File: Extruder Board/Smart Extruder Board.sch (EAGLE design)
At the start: 15 parts

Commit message: BCN3D Electronics REV.E tested and manufactured
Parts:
- removed FFC1: FFC_20V_90G_1MM", MarcEagleParts:FFC_20V_90G_1MM"
- removed HALL: (no value), adafruit:JST_3PIN
- removed HOTEND: (no value), MarcEagleParts:JST_4PIN
- removed TP1, TP2, TP3, TP4, TP7: TPB1,27, testpad:TPB1,27
- added CN1: (no value), MarcEagleParts:JST_4PINPA
- added ENDSTOP: (no value), SparkFun-Connectors:JST_2MM_MALE
- added VERT_FFC1: FFC_20V_90G_1MM3, MarcEagleParts:FFC_20V_90G_1MM3
- CFAN, LFAN: MF (none) -> JST (JAPAN SOLDERLESS TERMINALS); MPN (none) -> S2B-PH-SM4-TB(LF)(SN); OC_FARNELL (none) -> 9492615
- TP5, TP6, U$1, U$2, U$3: OC_FARNELL (none) -> unknown
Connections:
- removed net ATLVL: FFC1.20, HALL.2, TP4.TP
- new net GNDTHERM: CN1.4, VERT_FFC1.2
- new net Z-ENDSTOP: ENDSTOP.+, VERT_FFC1.20
- net +24V: now also CN1.1, VERT_FFC1.10, VERT_FFC1.12, VERT_FFC1.18, VERT_FFC1.19, VERT_FFC1.8; no longer FFC1.10, FFC1.12, FFC1.18, FFC1.19, FFC1.8, HOTEND.1
- net +5V: now also VERT_FFC1.1; no longer FFC1.1, HALL.3
- net GND: now also ENDSTOP.-, VERT_FFC1.11, VERT_FFC1.17, VERT_FFC1.4, VERT_FFC1.7, VERT_FFC1.9, VERT_FFC1.GND@1, VERT_FFC1.GND@2; no longer FFC1.11, FFC1.17, FFC1.2, FFC1.4, FFC1.7, FFC1.9, FFC1.GND@2, FFC1.GND|1, HALL.1, HOTEND.4, TP7.TP
- net HOTEND: now also CN1.2, VERT_FFC1.13, VERT_FFC1.14, VERT_FFC1.15, VERT_FFC1.16; no longer FFC1.13, FFC1.14, FFC1.15, FFC1.16, HOTEND.2, TP3.TP
- net HOTEND_THERM: now also CN1.3, VERT_FFC1.3; no longer FFC1.3, HOTEND.3, TP1.TP
- net LFAN: now also VERT_FFC1.5, VERT_FFC1.6; no longer FFC1.5, FFC1.6, TP2.TP
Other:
- note added: "D"
- note removed: "B"

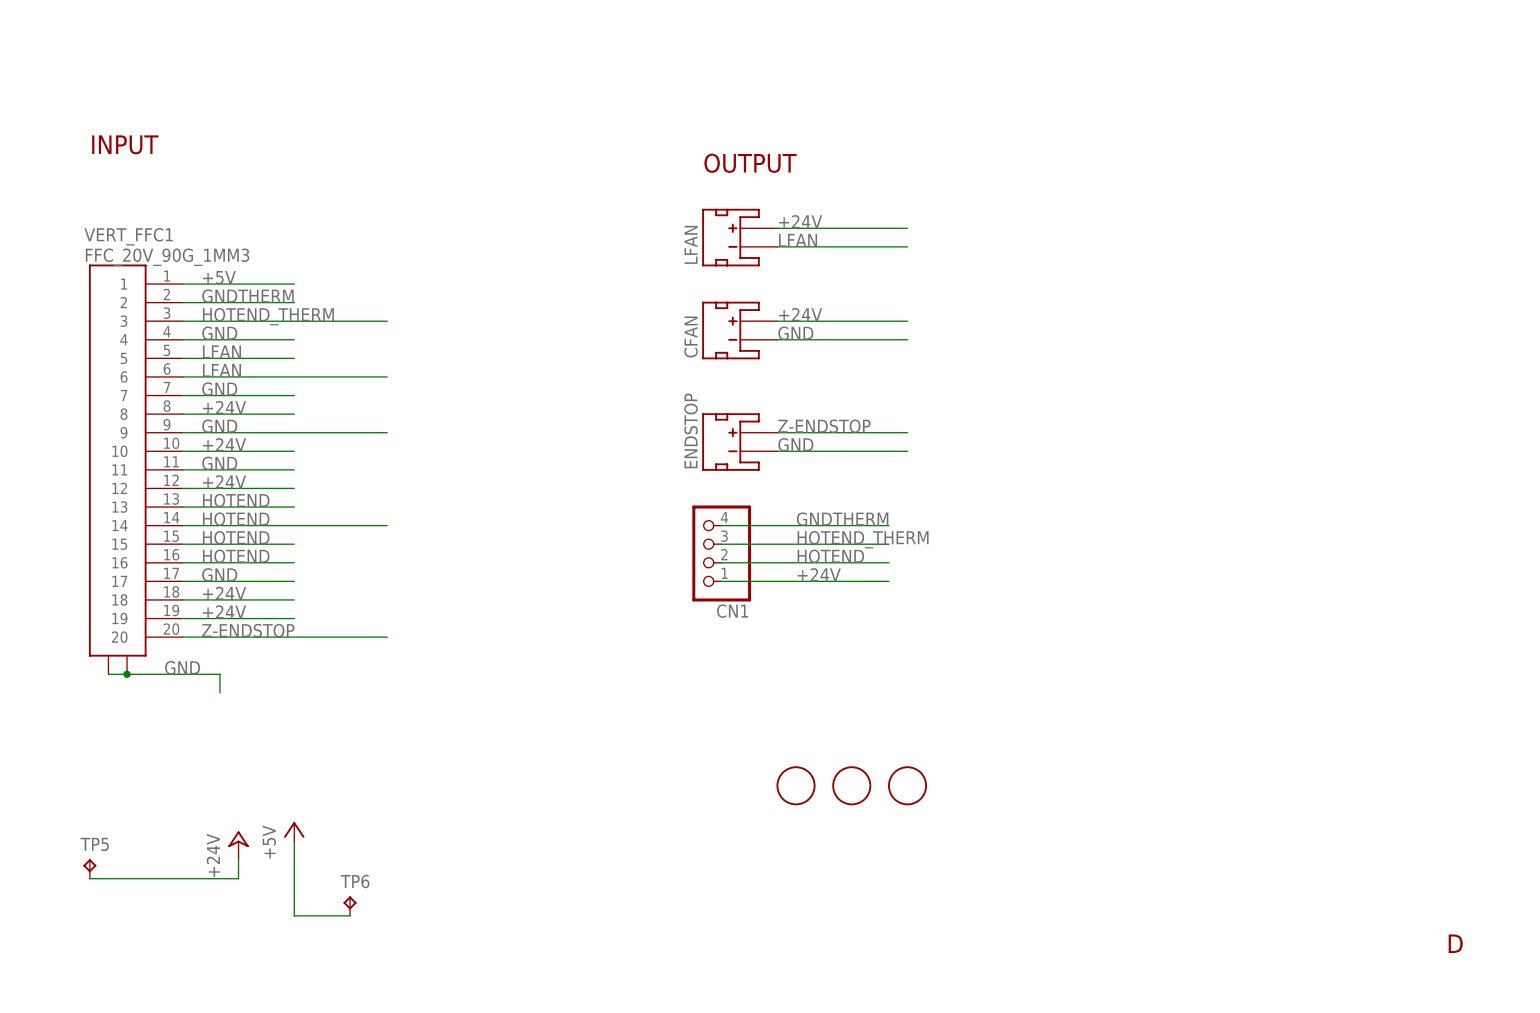
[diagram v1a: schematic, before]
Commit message: File for the REV.H
Files from the REV.H Released with new and more documentation.
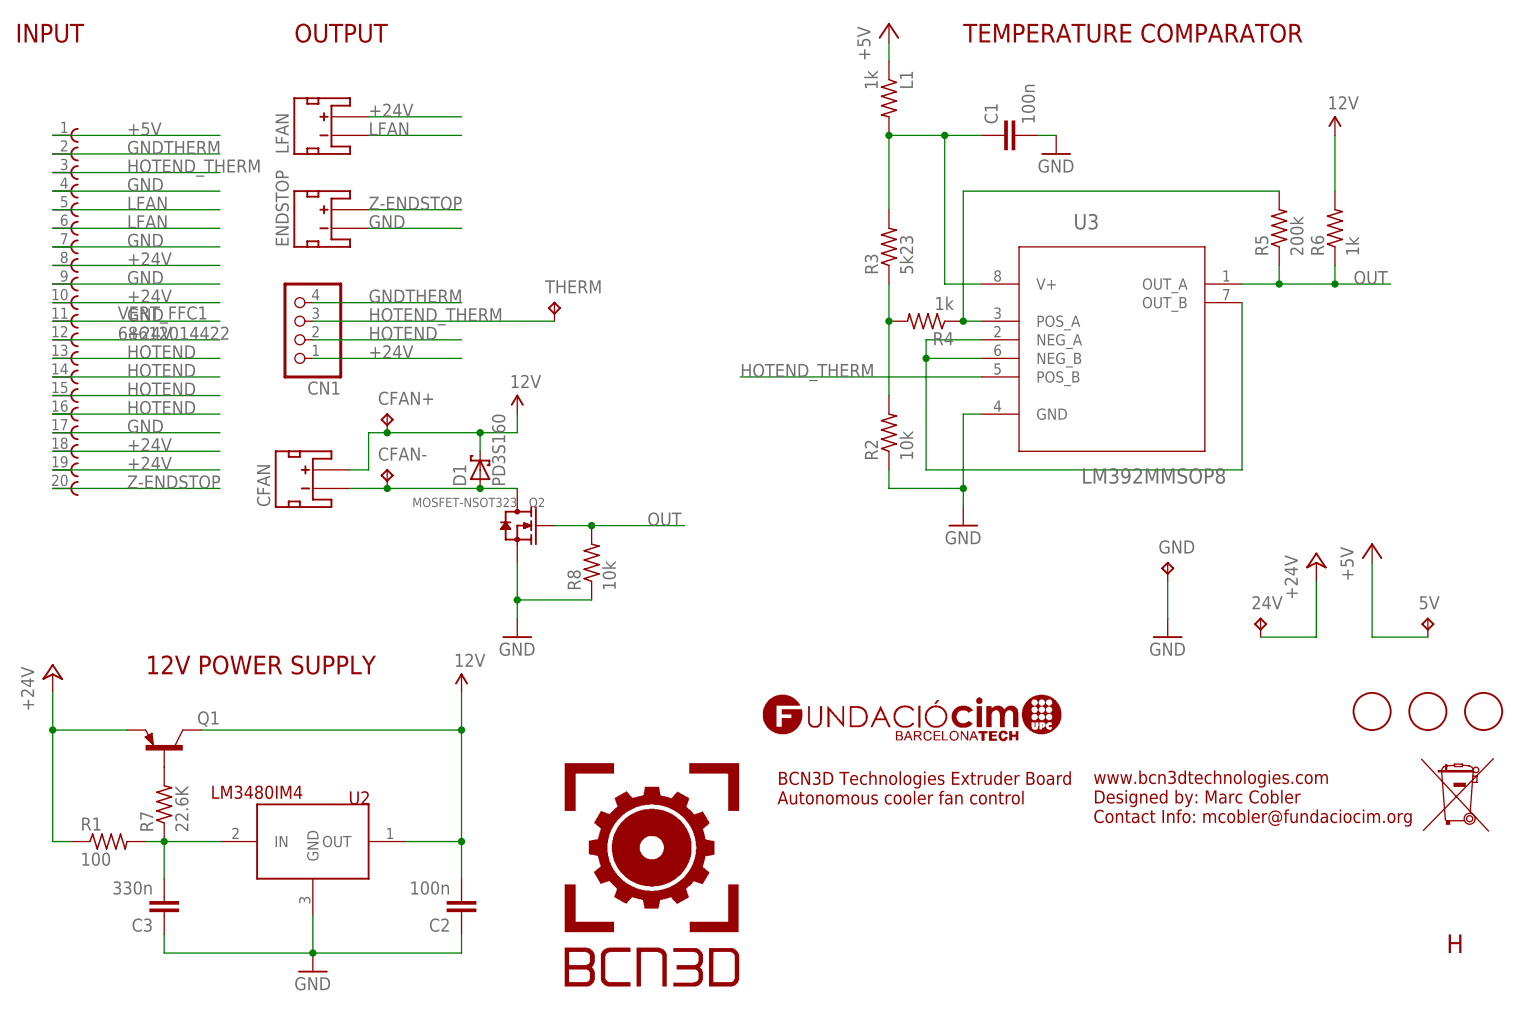
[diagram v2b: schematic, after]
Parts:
- removed TP5, TP6: TPB1,27, testpad:TPB1,27
- added 24V, 5V, CFAN+, CFAN-, GND, THERM: TPB1,27, testpad:TPB1,27
- added C1, C2: 100n, rcl:C-EUC0603K
- added C3: 330n, rcl:C-EUC0805
- added D1: PD3S160, diode:PD3S160
- added L1, R4, R6: 1k, rcl:R-US_R0603
- added Q1: BC807W, transistor-pnp:BC807W
- added Q2: MOSFET-NSOT323, MarcEagleParts:MOSFET-NSOT323
- added R1: 100, rcl:R-US_R1210
- added R2, R8: 10k, rcl:R-US_R0603
- added R3: 5k23, rcl:R-US_R0603
- added R5: 200k, rcl:R-US_R0603
- added R7: 22.6K, rcl:R-US_R0603
- added U2: LM3480IM4, SparkFun-PowerIC:LM3480IM4
- added U3: LM392MMSOP8, MarcEagleParts:LM392MMSOP8
- CN1: MF (none) -> JST (JAPAN SOLDERLESS TERMINALS); MPN (none) -> SM04B-PASS-TBT(LF)(SN); OC_FARNELL unknown -> 2399347
- VERT_FFC1: value FFC_20V_90G_1MM3 -> 68612014422; device MarcEagleParts:FFC_20V_90G_1MM3 -> FPC_FFC_Connectors_:68612014422
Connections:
- new net 12V: C2.2, CFAN+.TP, CFAN.+, D1.C, Q1.C, R6.2, U2.OUT
- new net DRAIN: CFAN-.TP, CFAN.-, D1.A, Q2.D
- new net IN: C3.2, R1.2, R7.1, U2.IN
- new net N$1: Q1.B, R7.2
- new net N$2: C1.1, L1.2, R3.2, U3.V+
- new net N$3: U3.NEG_A, U3.NEG_B, U3.OUT_B
- new net N$4: R2.2, R3.1, R4.2
- new net N$5: R4.1, R5.2, U3.POS_A
- new net OUT: Q2.G, R5.1, R6.1, R8.2, U3.OUT_A
- net +24V: now also 24V.TP, Q1.E, R1.1; no longer CFAN.+, TP5.TP
- net +5V: now also 5V.TP, L1.1; no longer TP6.TP
- net GND: now also C1.2, C2.1, C3.1, GND.TP, Q2.S, R2.1, R8.1, U2.GND, U3.GND; no longer CFAN.-, VERT_FFC1.GND@1, VERT_FFC1.GND@2
- net HOTEND_THERM: now also THERM.TP, U3.POS_B
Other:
- note added: "12V POWER SUPPLY"
- note added: "BCN3D Technologies Extruder Board Autonomous cooler fan control"
- note added: "H"
- note added: "TEMPERATURE COMPARATOR"
- note added: "www.bcn3dtechnologies.com Designed by: Marc Cobler Contact Info: mcobler@fundaciocim.org"
- note removed: "D"
- moved on the sheet: CFAN, CN1, ENDSTOP, LFAN
